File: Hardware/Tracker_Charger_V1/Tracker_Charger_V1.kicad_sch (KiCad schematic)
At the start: 52 parts, among them J1 USB_C_USB20, J2 GSB3CN1130DSHR, J3 GSB3CN1130DSHR, J4 GSB3CN1130DSHR, J5 SSD1306_I2C_128x64, J6 GSB3CN1130DSHR, J7 GSB3CN1130DSHR, SW1 SW_Push, SW2 SW_Push, SW3 SW_Push, SW4 SW_Push, SW5 SW_Push, SW6 SW_Push, U1 ESP32-C3-MINI-1-N4, U2 IN-PI15TAT5R5G5B, U3 RT8010, U6 IN-PI15TAT5R5G5B, U7 IN-PI15TAT5R5G5B, U8 IN-PI15TAT5R5G5B, U9 IN-PI15TAT5R5G5B

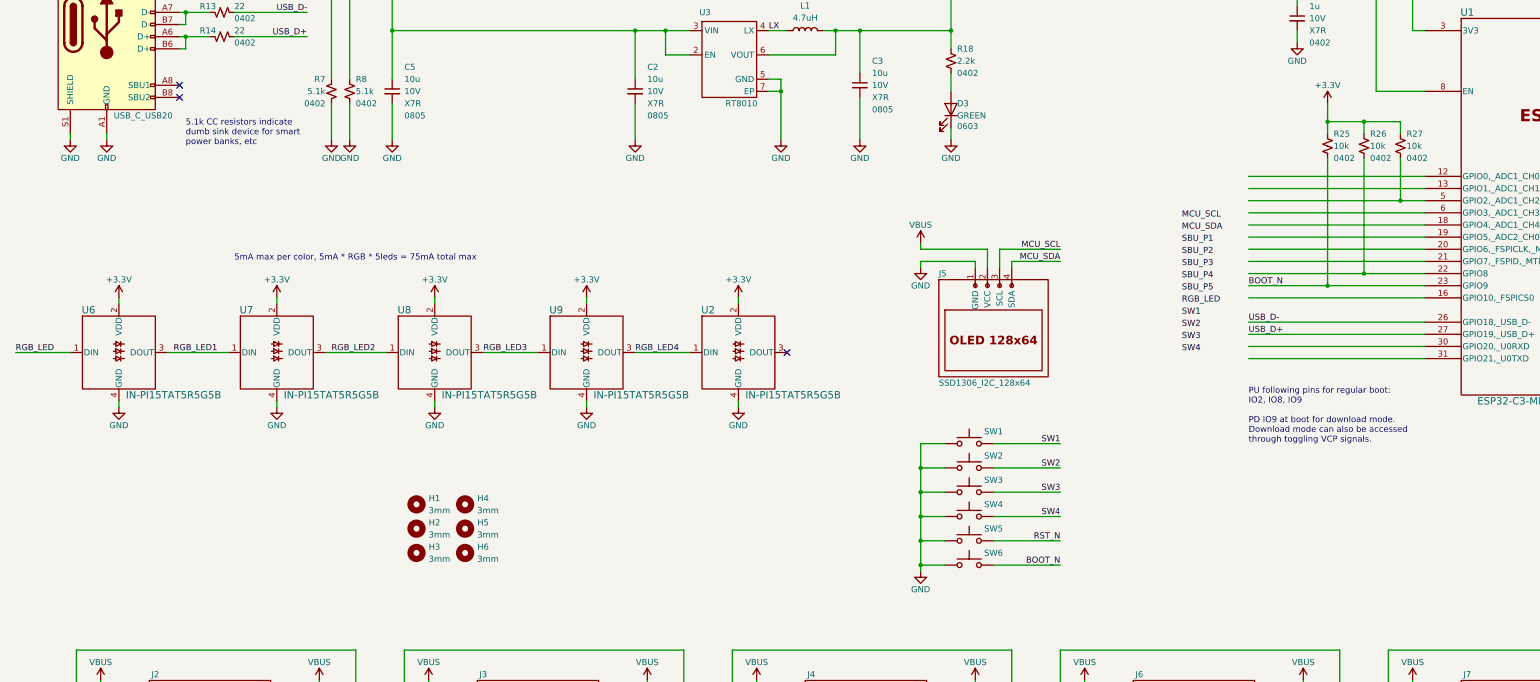
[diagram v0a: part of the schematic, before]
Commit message: Updated/Added Footprints
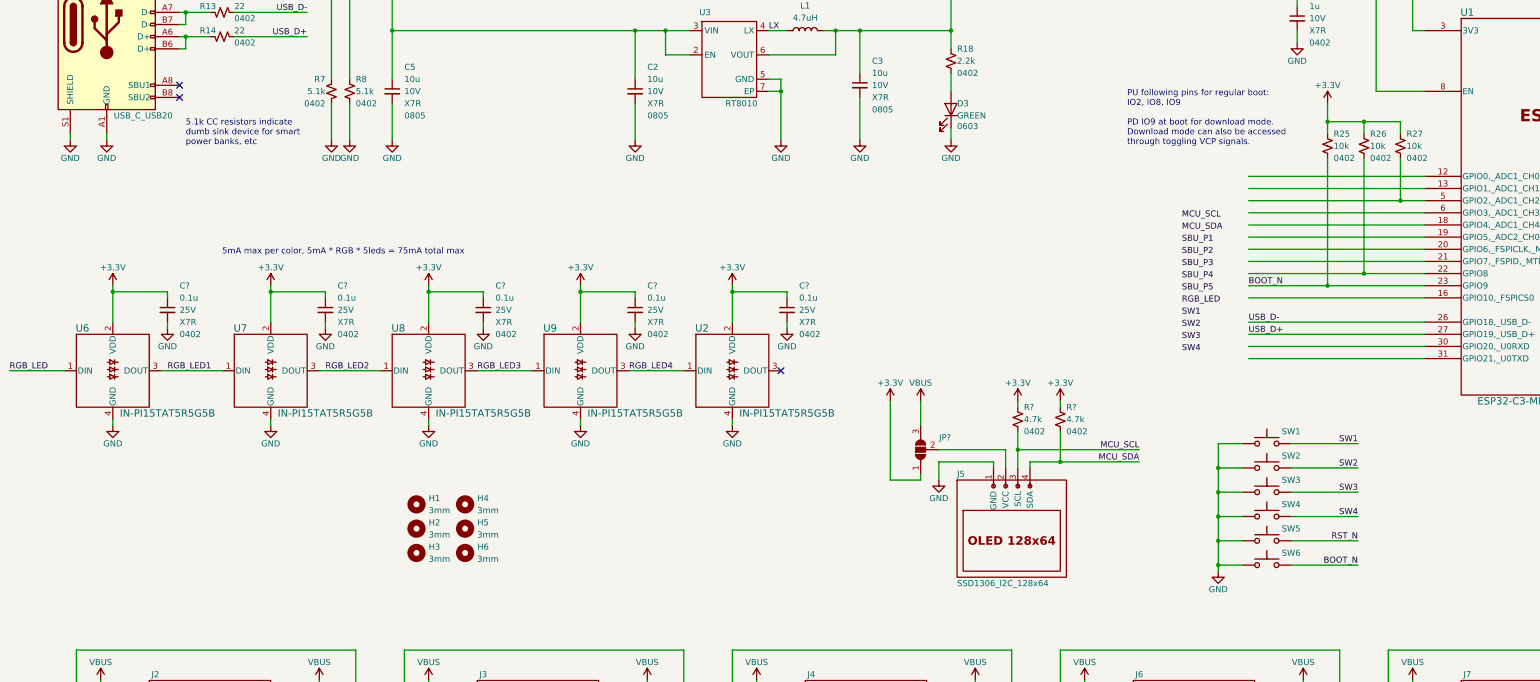
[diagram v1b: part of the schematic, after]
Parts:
- added C? (x5): 0.1u, Capacitor_SMD:C_0402_1005Metric, symbol Device:C_Small
- added JP?: SolderJumper_3_Open, symbol Jumper:SolderJumper_3_Open
- added R? (x2): 4.7k, Resistor_SMD:R_0402_1005Metric, symbol Device:R_Small_US
- J5: footprint Display:SSD1306_12864_I2C -> 00_tracker_fp:SSD1306_12864_I2C_13in
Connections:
- net +3.3V: now also C?.1, C?.1, C?.1, C?.1, C?.1, JP?.1 (A), R?.1, R?.1
- net GND: now also C?.2, C?.2, C?.2, C?.2, C?.2
- net MCU_SCL: now also R?.2
- net MCU_SDA: now also R?.2
- net VBUS: now also JP?.3 (B); no longer J5.2 (VCC)
- new net: J5.2 (VCC), JP?.2 (C)
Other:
- moved on the sheet: J5, SW1, SW2, SW3, SW4, SW5, SW6, U2, U6, U7, U8, U9

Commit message: Changed Charger PCB MCU to STM32
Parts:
- removed U1: ESP32-C3-MINI-1-N4, 00_tracker_fp:ESP32-C3-MINI-1_EXP, symbol 00_tracker_sym:ESP32-C3-MINI-1-N4
- added C11, C8: 10u, Capacitor_SMD:C_0805_2012Metric, symbol Device:C_Small
- added C12, C14: 47p, Capacitor_SMD:C_0402_1005Metric, symbol Device:C_Small
- added C13, C15, C16, C17, C18, C19, C20, C21: 0.1u, Capacitor_SMD:C_0402_1005Metric, symbol Device:C_Small
- added C22, C23: 27p, Capacitor_SMD:C_0402_1005Metric, symbol Device:C_Small
- added C24: 1u, Capacitor_SMD:C_0402_1005Metric, symbol Device:C_Small
- added D1: GREEN, LED_SMD:LED_0603_1608Metric, symbol Device:LED
- added FB1: 600@100MHz, Resistor_SMD:R_0402_1005Metric, symbol Device:FerriteBead_Small
- added J8: ST-LINK, Connector_PinHeader_2.54mm:PinHeader_1x06_P2.54mm_Vertical, symbol Connector_Generic:Conn_01x06
- added JP2, JP? (x9): SolderJumper_2_Open, Jumper:SolderJumper-2_P1.3mm_Open_RoundedPad1.0x1.5mm, symbol Jumper:SolderJumper_2_Open
- added L2: 4.7uH, Inductor_SMD:L_Taiyo-Yuden_NR-30xx, symbol Device:L
- added R19, R20, R23, R24: 330, Resistor_SMD:R_0402_1005Metric, symbol Device:R_Small_US
- added R21, R22: 1k, Resistor_SMD:R_0402_1005Metric, symbol Device:R_Small_US
- added U1: FT234XD-T, Package_DFN_QFN:DFN-12-1EP_3x3mm_P0.45mm_EP1.66x2.38mm, symbol 00_tracker_sym:FT234XD-T
- added U4: STM32G070CBTx, Package_QFP:LQFP-48_7x7mm_P0.5mm, symbol MCU_ST_STM32G0:STM32G070CBTx
- added Y1: 8MHz, Crystal:Crystal_SMD_Abracon_ABM8G-4Pin_3.2x2.5mm, symbol Device:Crystal_GND24_Small
- C1: value 1u -> 0.1u; Voltage 10V -> 25V
- JP1: renamed from JP?; footprint (none) -> Jumper:SolderJumper-3_P1.3mm_Open_RoundedPad1.0x1.5mm_NumberLabels
- R18: value 2.2k -> 1k
- R25, R26, R27: value 10k -> 330
- gave numbers to parts that had none: 7
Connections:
- net +3.3V: now also C24.1, C8.1, J8.1 (Pin_1), L2.2, U4.5 (VREF+), U4.6 (VDD); no longer C3.1, L1.2, R25.1, R26.1, R27.1, U3.6 (VOUT)
- net GND: now also SW6.2, C11.2, C12.2, C13.2, C14.2, C15.2, C16.2, C17.2, C18.2, C19.2, C20.2, C21.2, C22.1, C23.2, C24.2, C8.2, J8.3 (Pin_3), U1.13 (GND__1), U1.5 (GND), U4.7 (VSS), Y1.2, Y1.4; no longer SW6.1
- net SW1: now also C20.1
- net SW2: now also C19.1
- net SW3: now also C18.1
- net SW4: now also C17.1
- net USB_D+: now also J1.A6 (D+), J1.B6 (D+), R14.1, C12.1; no longer R14.2
- net USB_D-: now also J1.A7 (D-), J1.B7 (D-), R13.1, C14.1; no longer R13.2
- net VBUS: now also FB1.1
- net at R26.2: now also JP?.2 (B)
- net at R27.2: now also JP?.2 (B)
- net BOOT_N: no longer names the net of R25.2
- net BOOT_N: now also JP?.2 (B); no longer SW6.2
- net RST_N renamed SW5
- net SW5: no longer R1.2
- new net: R25.1, U4.33 (PA11/PA9)
- new net: D1.1 (K), U1.6 (CBUS0)
- new net: D1.2 (A), R22.2
- new net: C13.1, C15.1, R21.1, R22.1, U1.3 (3V3OUT), U1.9 (VCCIO)
- new net: R19.1, U1.7 (TXD)
- new net: C3.1, L1.2, L2.1, U3.6 (VOUT)
- new net: R23.1, U4.11 (PA0)
- new net: JP2.2 (B), R23.2
- new net: JP2.1 (A), JP?.1 (A), U4.12 (PA1)
- new net: JP?.1 (A), JP?.1 (A), U4.23 (PB11)
- new net: JP?.1 (A), JP?.1 (A), U4.19 (PB0)
- new net: R26.1, U4.21 (PB2)
- new net: R27.1, U4.22 (PB10)
- new net: JP?.1 (A), JP?.1 (A), U4.34 (PA12/PA10)
- new net: R24.1, U4.45 (PB6)
- new net: JP?.1 (A), JP?.1 (A), U4.46 (PB7)
- new net: R20.1, U1.10 (RXD)
- new net: R14.2, U1.12 (USBDP)
- new net: R13.2, U1.1 (USBDM)
- new net: C16.1, R21.2, U1.2 (~{RESET}#)
- new net: C11.1, FB1.2, U1.4 (VCC)
- new net: JP?.2 (B), R24.2
- new net MCU_NRST: C21.1, J8.5 (Pin_5), R1.2, SW6.1, U4.10 (NRST)
- new net MCU_XI: C22.2, U4.8 (PF0), Y1.3
- new net MCU_XO: C23.1, U4.9 (PF1), Y1.1
- new net ST_SWCLK: J8.2 (Pin_2), U4.36 (PA14)
- new net ST_SWDIO: J8.4 (Pin_4), U4.35 (PA13)
- new net VCP_RX: R20.2, U4.13 (PA2)
- new net VCP_TX: R19.2, U4.14 (PA3)
- no-connect marks 3 -> 7
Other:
- note added: "USART1"
- note added: "USART2"
- note added: "USART3"
- note added: "USART4"
- note removed: "Evaluated ~120mA average, 500mA peak"
- note removed: "PU following pins for regular boot: IO2, IO8, IO9 PD IO9 at boot for download mode. Download mode can also be accessed through toggling VCP signals."
- moved on the sheet: C10, C2, C3, C4, C5, C6, C7, C9, D3, H1, H2, H3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

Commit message: Charger PCB Update
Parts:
- removed H1, H2, H3, H4, H5, H6: 3mm, MountingHole:MountingHole_3mm_Pad_Via, symbol Mechanical:MountingHole
- removed JP2, JP? (x9): SolderJumper_2_Open, Jumper:SolderJumper-2_P1.3mm_Open_RoundedPad1.0x1.5mm, symbol Jumper:SolderJumper_2_Open
- added D2: GREEN, LED_SMD:LED_0603_1608Metric, symbol Device:LED
- added H1, H2, H3, H4, H5, H6: 3mm, MountingHole:MountingHole_3mm_Pad_Via, symbol Mechanical:MountingHole_Pad
- added JP2, JP3, JP4, JP5, JP6: SolderJumper_3_Open, Jumper:SolderJumper-3_P1.3mm_Open_RoundedPad1.0x1.5mm_NumberLabels, symbol Jumper:SolderJumper_3_Open
- added R28: 1k, Resistor_SMD:R_0402_1005Metric, symbol Device:R_Small_US
- J2, J3, J4, J6, J7: footprint 00_tracker_fp:AMPHENOL_GSB3CN1130DSHR -> 00_tracker_fp:AMPHENOL_GSB3CN1130DSHR_NEW1
- J8: footprint Connector_PinHeader_2.54mm:PinHeader_1x06_P2.54mm_Vertical -> Connector_PinHeader_2.54mm:PinHeader_1x06_P2.54mm_Horizontal
- R10, R11, R12, R15, R2, R3, R4, R5, R6, R9: value 1k -> 330
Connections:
- net GND: now also D2.1 (K)
- net VBUS: now also R28.1
- net BAND_TX1: now reaches U4.33 (PA11/PA9)
- net BAND_TX1: now also R2.1, R3.2, JP2.3 (B); no longer R25.1
- net at R25.2: now also J7.B8 (SBU2)
- net at J6.A8 (SBU1): now also R23.1; no longer R11.1
- net at J3.A8 (SBU1): now also R6.1; no longer R5.1
- net at J6.B6 (DP2): now also JP5.1 (A)
- net at J6.B8 (SBU2): now also R15.2; no longer R10.1
- net at R12.1: now also JP4.2 (C); no longer J7.B8 (SBU2)
- net 3V3_RAW: now reaches C3.1, L1.2, L2.1, U3.6 (VOUT)
- net BAND_TX4: now reaches U4.11 (PA0)
- net BAND_TX4: now also R15.1, R23.2, JP5.3 (B); no longer R23.1
- net BAND_RX4: now reaches U4.12 (PA1)
- net BAND_RX4: now also R24.2
- net at J7.A8 (SBU1): now also R26.1; no longer R15.1
- net at J7.B6 (DP2): now also JP6.1 (A)
- net BAND_RX2: now reaches U4.23 (PB11)
- net BAND_RX2: now also R9.2
- net at J3.B6 (DP2): now also JP3.1 (A)
- net at J3.B8 (SBU2): now also R5.2; no longer R4.1
- net BAND_RX3: now reaches U4.19 (PB0)
- net BAND_RX3: now also R12.2
- net BAND_TX3: now reaches U4.21 (PB2)
- net BAND_TX3: now also R10.1, R11.2, JP4.3 (B); no longer R26.1
- net at R27.1: now also JP6.2 (C); no longer U4.22 (PB10)
- net BAND_RX1: now reaches U4.34 (PA12/PA10)
- net BAND_RX1: now also R4.2
- net at R24.1: now also JP5.2 (C); no longer U4.45 (PB6)
- net BAND_RX5: now reaches U4.46 (PB7)
- net BAND_RX5: now also R27.2
- net at R9.1: now also JP3.2 (C); no longer J4.A8 (SBU1)
- net at J4.B6 (DP2): now also JP4.1 (A)
- net at J4.B8 (SBU2): now also R10.2; no longer R6.1
- net BAND_TX5: now reaches R26.2
- net BAND_TX5: now also R25.1, U4.45 (PB6), JP6.3 (B)
- net at J2.B6 (DP2): now also JP2.1 (A)
- net at J2.B8 (SBU2): now also R2.2; no longer R2.1
- removed net SBU_P1: R2.2, R3.2
- removed net SBU_P2: R4.2, R5.2
- net SBU_P3 renamed BAND_TX2
- net BAND_TX2: now also R5.1, U4.22 (PB10), JP3.3 (B); no longer R9.2
- removed net SBU_P4: R10.2, R11.2
- removed net SBU_P5: R12.2, R15.2
- new net: D2.2 (A), R28.2
- new net: JP2.2 (C), R4.1
- new net: J4.A8 (SBU1), R11.1
- no-connect marks 7 -> 13
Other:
- moved on the sheet: C2, C22, C23, C3, C8, D3, J2, J3, J4, J6, J7, L1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

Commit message: SCH & PCB Updated
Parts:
- removed J8: ST-LINK, Connector_PinHeader_2.54mm:PinHeader_1x06_P2.54mm_Horizontal, symbol Connector_Generic:Conn_01x06
- added C25, C26, C27, C28, C29, C30, C31, C32, C33, C34, C35, C36, C37, C38, C39, C40, C41, C42, C43, C44, C45, C46, C47, C48, C49: 0.1u, Capacitor_SMD:C_0402_1005Metric, symbol Device:C_Small
- added C50: 1u, Capacitor_SMD:C_0402_1005Metric, symbol Device:C_Small
- added FB2: 600@100MHz, Resistor_SMD:R_0402_1005Metric, symbol Device:FerriteBead_Small
- added J8: ST-LINK, Connector_PinHeader_2.54mm:PinHeader_1x08_P2.54mm_Horizontal, symbol Connector:Conn_01x08_Pin
- added R29, R31, R33, R35, R37: 33m, Resistor_SMD:R_1206_3216Metric, symbol Device:R_Small_US
- added R30, R32, R34, R36, R38: 10k, Resistor_SMD:R_0402_1005Metric, symbol Device:R_Small_US
- added R39, R40, R41, R42, R43: 100k, Resistor_SMD:R_0402_1005Metric, symbol Device:R_Small_US
- added U10, U11, U12, U13, U5: INA180A3, Package_TO_SOT_SMD:SOT-23-5, symbol Amplifier_Current:INA180A3
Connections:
- net +3.3V: now also JP1.3 (B), FB2.1, J8.1 (Pin_1); no longer JP1.1 (A), U4.5 (VREF+)
- net GND: now also C25.2, C27.2, C28.2, C29.2, C30.2, C32.2, C33.2, C34.2, C35.2, C37.2, C38.2, C39.2, C40.2, C42.2, C43.2, C44.2, C45.2, C47.2, C48.2, C49.2, C50.2, J8.3 (Pin_3), J8.6 (Pin_6), U10.2 (GND), U11.2 (GND), U12.2 (GND), U13.2 (GND), U5.2 (GND)
- net MCU_NRST: now also J8.5 (Pin_5)
- net MCU_SCL: now also U4.47 (PB8), J8.7 (Pin_7)
- net MCU_SDA: now also U4.48 (PB9), J8.8 (Pin_8)
- net RGB_LED: now also U4.44 (PB5)
- net ST_SWCLK: now also J8.2 (Pin_2)
- net ST_SWDIO: now also J8.4 (Pin_4)
- net SW1: now also U4.43 (PB4)
- net SW2: now also U4.42 (PB3)
- net SW3: now also U4.39 (PD1)
- net SW4: now also U4.40 (PD2)
- net SW5: now also U4.41 (PD3)
- net VBUS: now also JP1.1 (A), C25.1, C26.1, C28.1, C30.1, C31.1, C33.1, C35.1, C36.1, C38.1, C40.1, C41.1, C43.1, C45.1, C46.1, C48.1, R29.1, R31.1, R33.1, R35.1, R37.1, U10.3 (+), U10.5 (V+), U11.3 (+), U11.5 (V+), U12.3 (+), U12.5 (V+), U13.3 (+), U13.5 (V+), U5.3 (+), U5.5 (V+); no longer J2.A4 (VBUS_A), J2.A9 (VBUS_A__1), J2.B4 (VBUS_B), J2.B9 (VBUS_B__1), J3.A4 (VBUS_A), J3.A9 (VBUS_A__1), J3.B4 (VBUS_B), J3.B9 (VBUS_B__1), J4.A4 (VBUS_A), J4.A9 (VBUS_A__1), J4.B4 (VBUS_B), J4.B9 (VBUS_B__1), J6.A4 (VBUS_A), J6.A9 (VBUS_A__1), J6.B4 (VBUS_B), J6.B9 (VBUS_B__1), J7.A4 (VBUS_A), J7.A9 (VBUS_A__1), J7.B4 (VBUS_B), J7.B9 (VBUS_B__1), JP1.3 (B)
- net PRES4: now reaches J6.A5 (CC1)
- net PRES4: now also U4.27 (PB15), R42.2
- net PRES5: now reaches J7.A5 (CC1)
- net PRES5: now also U4.1 (PC13), R43.2
- net PRES2: now reaches J3.A5 (CC1)
- net PRES2: now also U4.26 (PB14), R40.2
- net I_SENS5: now reaches U4.15 (PA4)
- net I_SENS5: now also C49.1, R38.1
- net I_SENS4: now reaches U4.16 (PA5)
- net I_SENS4: now also C44.1, R36.1
- net I_SENS3: now reaches U4.17 (PA6)
- net I_SENS3: now also C39.1, R34.1
- net I_SENS2: now reaches U4.18 (PA7)
- net I_SENS2: now also C34.1, R32.1
- net I_SENS1: now reaches U4.24 (PB12)
- net I_SENS1: now also C29.1, R30.1
- net PRES3: now reaches U4.25 (PB13)
- net PRES3: now also J4.A5 (CC1), R41.2
- net PRES1: now reaches U4.28 (PA8)
- net PRES1: now also J2.B5 (CC2), R39.2
- new net: R36.2, U12.1
- new net: R30.2, U5.1
- new net: R32.2, U10.1
- new net: C50.1, FB2.2, U4.5 (VREF+)
- new net: R34.2, U11.1
- new net: R38.2, U13.1
- new net VBUS1: C26.2, C27.1, J2.A4 (VBUS_A), J2.A9 (VBUS_A__1), J2.B4 (VBUS_B), J2.B9 (VBUS_B__1), R29.2, R39.1, U5.4 (-)
- new net VBUS2: C31.2, C32.1, J3.A4 (VBUS_A), J3.A9 (VBUS_A__1), J3.B4 (VBUS_B), J3.B9 (VBUS_B__1), R31.2, R40.1, U10.4 (-)
- new net VBUS3: C36.2, C37.1, J4.A4 (VBUS_A), J4.A9 (VBUS_A__1), J4.B4 (VBUS_B), J4.B9 (VBUS_B__1), R33.2, R41.1, U11.4 (-)
- new net VBUS4: C41.2, C42.1, J6.A4 (VBUS_A), J6.A9 (VBUS_A__1), J6.B4 (VBUS_B), J6.B9 (VBUS_B__1), R35.2, R42.1, U12.4 (-)
- new net VBUS5: C46.2, C47.1, J7.A4 (VBUS_A), J7.A9 (VBUS_A__1), J7.B4 (VBUS_B), J7.B9 (VBUS_B__1), R37.2, R43.1, U13.4 (-)
- no-connect marks 13 -> 72
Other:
- note added: "A3 varient of INA180 = 100V/V @1A = 33mV drop, 3.3V full scale output Max Rsense Pd @3A = 0.3W"
- note added: "I2C1"
- moved on the sheet: C1, C17, C18, C19, C20, C24, J2, J3, J4, J5, J6, J7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

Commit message: PCB Layout Finalized
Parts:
- added LG2: ~, 00_tracker_fp:run_silk_14mm, symbol 00_tracker_sym:LOGO_MISC
- added LG3: ~, 00_tracker_fp:bench_silk_14mm, symbol 00_tracker_sym:LOGO_MISC
- added LG5: ~, 00_tracker_fp:hike_silk_14mm, symbol 00_tracker_sym:LOGO_MISC
- added LG6: ~, 00_tracker_fp:squat_silk_14mm, symbol 00_tracker_sym:LOGO_MISC
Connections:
- net +3.3V: now also D3.2 (A), J8.8 (Pin_8); no longer J8.1 (Pin_1), R18.1
- net GND: now also J8.2 (Pin_2), J8.5 (Pin_5), R18.2; no longer D3.1 (K), J8.3 (Pin_3), J8.6 (Pin_6)
- net MCU_NRST: now also J8.4 (Pin_4); no longer J8.5 (Pin_5)
- net MCU_SCL: now also J8.6 (Pin_6); no longer J8.7 (Pin_7)
- net MCU_SDA: now also J8.7 (Pin_7); no longer J8.8 (Pin_8)
- net PRES5: now also U4.38 (PD0); no longer U4.1 (PC13)
- net ST_SWCLK: now also J8.1 (Pin_1); no longer J8.2 (Pin_2)
- net ST_SWDIO: now also J8.3 (Pin_3); no longer J8.4 (Pin_4)
- net SW3: now also C17.1, U4.40 (PD2); no longer C18.1, U4.39 (PD1)
- net SW4: now also C18.1, U4.39 (PD1); no longer C17.1, U4.40 (PD2)
- new net: D3.1 (K), R18.1
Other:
- title: SilhouetteSync V1 -> SilhouetteSync Charger V1
- moved on the sheet: D3, J8, LG1, R18, SW3, SW4
